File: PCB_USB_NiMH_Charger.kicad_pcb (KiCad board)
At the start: 2 copper layers, 94.9 x 72 mm, 53 parts, among them J1 USB_C_Receptacle_Simple, J2 Conn_02x01, Q1 2SA1015, Q2 2SB834, Q3 2SB834, Q4 2SB834, Q5 2SB834, U1 LM339, U2 S-812C33A_TO92

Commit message: 配線調整
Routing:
- net +5V: track 414.1 -> 427.6 mm
- net GND: track 171.0 -> 174.4 mm
- net Net-(R14-Pad1): track 64.1 -> 65.2 mm
- net Net-(BT3-+): track 64.0 -> 64.8 mm

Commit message: 抵抗値を変更
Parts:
- R11, R7: value 2k -> 2.7k
- R15, R19: value 2k -> 1.6k
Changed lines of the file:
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@@
         (effects (font (size 1 1) (thickness 0.15)))
     )
-    (fp_text value "2k" (at 2.54 1.92) (layer "F.Fab")
+    (fp_text value "1.6k" (at 2.54 1.92) (layer "F.Fab")
         (effects (font (size 1 1) (thickness 0.15)))
     )
@@
         (effects (font (size 1 1) (thickness 0.15)))
     )
-    (fp_text value "2k" (at 2.54 1.92) (layer "F.Fab")
+    (fp_text value "2.7k" (at 2.54 1.92) (layer "F.Fab")
         (effects (font (size 1 1) (thickness 0.15)))
     )
@@
         (effects (font (size 1 1) (thickness 0.15)))
     )
-    (fp_text value "2k" (at 2.54 1.92) (layer "F.Fab")
+    (fp_text value "1.6k" (at 2.54 1.92) (layer "F.Fab")
         (effects (font (size 1 1) (thickness 0.15)))
     )
@@
         (effects (font (size 1 1) (thickness 0.15)))
     )
-    (fp_text value "2k" (at 2.54 1.92) (layer "F.Fab")
-        (effects (font (size 1 1) (thickness 0.15)))
-    )
+    (fp_text value "2.7k" (at 2.54 1.92) (layer "F.Fab")
+        (effects (font (size 1 1) (thickness 0.15)))
+    )

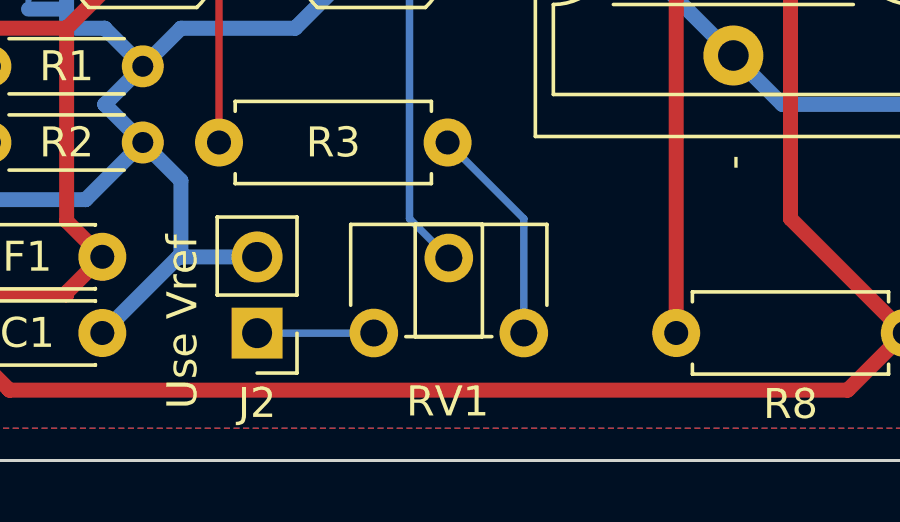
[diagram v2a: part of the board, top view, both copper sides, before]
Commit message: 半固定抵抗のフットプリントを修正
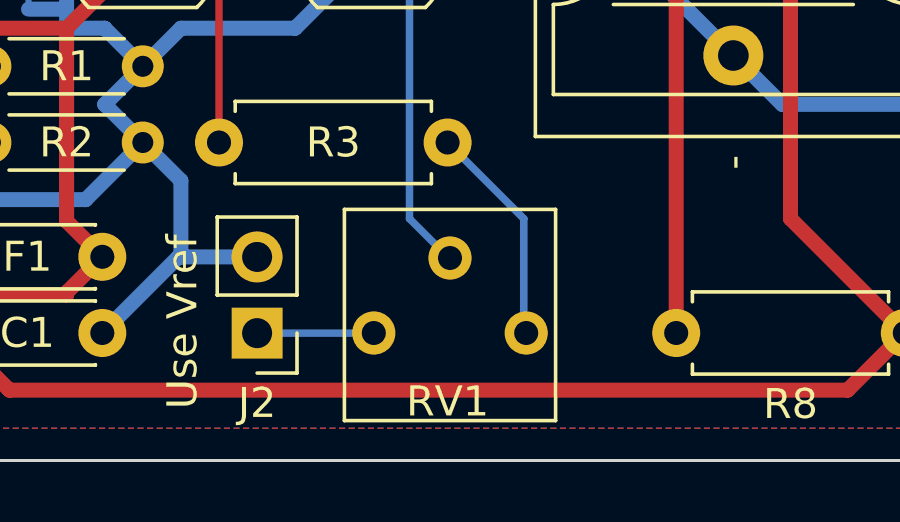
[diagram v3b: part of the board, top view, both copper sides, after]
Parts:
- RV1: footprint Potentiometer_THT:Potentiometer_ACP_CA6-H2,5_Horizontal -> mylib:Potentiometer_TOCOS_GF063P_Vertical
- turned RV1 to 0 degrees
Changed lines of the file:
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@@
     )
   )
-  (footprint "Potentiometer_THT:Potentiometer_ACP_CA6-H2,5_Horizontal" (layer "F.Cu")
-    (at 48.34 123.19 90)
-    (descr "Potentiometer, horizontal, ACP CA6-H2,5, http://www.acptechnologies.com/wp-content/uploads/2017/06/01-ACP-CA6.pdf")
-    (tags "Potentiometer horizontal ACP CA6-H2,5")
+  (footprint "mylib:Potentiometer_TOCOS_GF063P_Vertical" (layer "F.Cu")
+    (at 48.34 123.19)
+    (descr "Potentiometer, vertical, TOCOS GF063P, https://www.tocos-j.co.jp/tocos-j-wp/wp-content/uploads/2019/06/GF063_Series-1.pdf")
+    (tags "Potentiometer vertical TOCOS GF063P")
     (property "Sheetfile" "PCB_USB_NiMH_Charger.kicad_sch")
     (property "Sheetname" "")
@@
     (property "ki_keywords" "resistor variable")
     (attr through_hole)
-    (fp_text reference "RV1" (at -2.286 2.46 180) (layer "F.SilkS")
+    (fp_text reference "RV1" (at 2.46 2.286) (layer "F.SilkS")
         (effects (font (size 1 1) (thickness 0.15)))
     )
-    (fp_text value "10k" (at 0 7.06 90) (layer "F.Fab")
+    (fp_text value "10k" (at 2.24 3.702) (layer "F.Fab")
         (effects (font (size 1 1) (thickness 0.15)))
     )
-    (fp_text user "${REFERENCE}" (at 1.75 2.5 90) (layer "F.Fab")
-        (effects (font (size 0.78 0.78) (thickness 0.15)))
+    (fp_text user "${REFERENCE}" (at 2.54 1.8) (layer "F.Fab")
+        (effects (font (size 1 1) (thickness 0.15)))
     )
-    (fp_line (start -0.121 1.066) (end -0.121 3.935)
+    (fp_line (start -0.98 -4.12) (end 6.06 -4.12)
       (stroke (width 0.12) (type solid)) (layer "F.SilkS"))
-    (fp_line (start -0.121 1.38) (end -0.121 3.62)
+    (fp_line (start -0.98 2.92) (end -0.98 -4.12)
       (stroke (width 0.12) (type solid)) (layer "F.SilkS"))
-    (fp_line (start -0.121 1.38) (end 3.62 1.38)
+    (fp_line (start -0.98 2.92) (end 6.06 2.92)
       (stroke (width 0.12) (type solid)) (layer "F.SilkS"))
-    (fp_line (start -0.121 3.62) (end 3.62 3.62)
+    (fp_line (start 6.06 2.92) (end 6.06 -4.12)
       (stroke (width 0.12) (type solid)) (layer "F.SilkS"))
-    (fp_line (start 0.925 -0.77) (end 3.62 -0.77)
-      (stroke (width 0.12) (type solid)) (layer "F.SilkS"))
-    (fp_line (start 0.925 5.77) (end 3.62 5.77)
-      (stroke (width 0.12) (type solid)) (layer "F.SilkS"))
-    (fp_line (start 3.62 -0.77) (end 3.62 5.77)
-      (stroke (width 0.12) (type solid)) (layer "F.SilkS"))
-    (fp_line (start 3.62 1.38) (end 3.62 3.62)
-      (stroke (width 0.12) (type solid)) (layer "F.SilkS"))
-    (fp_line (start -1.1 -1.1) (end -1.1 6.1)
+    (fp_line (start -1.12 -4.26) (end -1.12 3.09)
       (stroke (width 0.05) (type solid)) (layer "F.CrtYd"))
-    (fp_line (start -1.1 6.1) (end 3.75 6.1)
+    (fp_line (start -1.12 3.09) (end 6.23 3.09)
       (stroke (width 0.05) (type solid)) (layer "F.CrtYd"))
-    (fp_line (start 3.75 -1.1) (end -1.1 -1.1)
+    (fp_line (start 6.23 -4.26) (end -1.12 -4.26)
       (stroke (width 0.05) (type solid)) (layer "F.CrtYd"))
-    (fp_line (start 3.75 6.1) (end 3.75 -1.1)
+    (fp_line (start 6.23 3.09) (end 6.23 -4.26)
       (stroke (width 0.05) (type solid)) (layer "F.CrtYd"))
-    (fp_line (start 0 -0.65) (end 3.5 -0.65)
+    (fp_line (start -0.86 -4) (end -0.86 2.8)
       (stroke (width 0.1) (type solid)) (layer "F.Fab"))
-    (fp_line (start 0 1.5) (end 0 3.5)
+    (fp_line (start -0.86 2.8) (end 5.94 2.8)
       (stroke (width 0.1) (type solid)) (layer "F.Fab"))
-    (fp_line (start 0 3.5) (end 3.5 3.5)
+    (fp_line (start 1.339 -1.076) (end 2.464 -1.076)
       (stroke (width 0.1) (type solid)) (layer "F.Fab"))
-    (fp_line (start 0 5.65) (end 0 -0.65)
+    (fp_line (start 1.339 -0.924) (end 1.339 -1.076)
       (stroke (width 0.1) (type solid)) (layer "F.Fab"))
-    (fp_line (start 3.5 -0.65) (end 3.5 5.65)
+    (fp_line (start 2.464 -2.201) (end 2.616 -2.201)
       (stroke (width 0.1) (type solid)) (layer "F.Fab"))
-    (fp_line (start 3.5 1.5) (end 0 1.5)
+    (fp_line (start 2.464 -1.076) (end 2.464 -2.201)
       (stroke (width 0.1) (type solid)) (layer "F.Fab"))
-    (fp_line (start 3.5 3.5) (end 3.5 1.5)
+    (fp_line (start 2.464 -0.924) (end 1.339 -0.924)
       (stroke (width 0.1) (type solid)) (layer "F.Fab"))
-    (fp_line (start 3.5 5.65) (end 0 5.65)
+    (fp_line (start 2.464 0.201) (end 2.464 -0.924)
       (stroke (width 0.1) (type solid)) (layer "F.Fab"))
-    (pad "1" thru_hole circle (at 0 0 90) (size 1.62 1.62) (drill 0.9) (layers "*.Cu" "*.Mask")
+    (fp_line (start 2.616 -2.201) (end 2.616 -1.076)
+      (stroke (width 0.1) (type solid)) (layer "F.Fab"))
+    (fp_line (start 2.616 -1.076) (end 3.741 -1.076)
+      (stroke (width 0.1) (type solid)) (layer "F.Fab"))
+    (fp_line (start 2.616 -0.924) (end 2.616 0.201)
+      (stroke (width 0.1) (type solid)) (layer "F.Fab"))
+    (fp_line (start 2.616 0.201) (end 2.464 0.201)
+      (stroke (width 0.1) (type solid)) (layer "F.Fab"))
+    (fp_line (start 3.741 -1.076) (end 3.741 -0.924)
+      (stroke (width 0.1) (type solid)) (layer "F.Fab"))
+    (fp_line (start 3.741 -0.924) (end 2.616 -0.924)
+      (stroke (width 0.1) (type solid)) (layer "F.Fab"))
+    (fp_line (start 5.94 -4) (end -0.86 -4)
+      (stroke (width 0.1) (type solid)) (layer "F.Fab"))
+    (fp_line (start 5.94 2.8) (end 5.94 -4)
+      (stroke (width 0.1) (type solid)) (layer "F.Fab"))
+    (fp_circle (center 2.54 -1) (end 2.54 -2.5)
+      (stroke (width 0.1) (type solid)) (fill none) (layer "F.Fab"))
+    (pad "1" thru_hole circle (at 0 0 90) (size 1.44 1.44) (drill 0.8) (layers "*.Cu" "*.Mask")
       (net 10 "Net-(J2-Pin_1)") (pinfunction "1") (pintype "passive"))
-    (pad "2" thru_hole circle (at 2.5 2.5 90) (size 1.62 1.62) (drill 0.9) (layers "*.Cu" "*.Mask")
+    (pad "2" thru_hole circle (at 2.54 -2.5 90) (size 1.44 1.44) (drill 0.8) (layers "*.Cu" "*.Mask")
       (net 16 "Net-(Q1-B)") (pinfunction "2") (pintype "passive"))
-    (pad "3" thru_hole circle (at 0 5 90) (size 1.62 1.62) (drill 0.9) (layers "*.Cu" "*.Mask")
+    (pad "3" thru_hole circle (at 5.08 0 90) (size 1.44 1.44) (drill 0.8) (layers "*.Cu" "*.Mask")
       (net 32 "Net-(R3-Pad1)") (pinfunction "3") (pintype "passive"))
-    (model "${KICAD6_3DMODEL_DIR}/Potentiometer_THT.3dshapes/Potentiometer_ACP_CA6-H2,5_Horizontal.wrl"
-      (offset (xyz 0 0 0))
+    (model "${KICAD6_3DMODEL_DIR}/Potentiometer_THT.3dshapes/Potentiometer_Vishay_T73YP_Vertical.wrl"
+      (offset (xyz 2.3 -1.692 0))
       (scale (xyz 1 1 1))
       (rotate (xyz 0 0 0))
